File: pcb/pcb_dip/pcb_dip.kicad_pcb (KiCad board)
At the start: 2 copper layers, 67.3 x 43.2 mm, 20 parts, among them J1 USB_B_Micro, J4 Barrel_Jack, SW1 MODE, SW2 UP, SW3 DOWN, U1 ATmega328P-PU, U2 MPXV5010, U3 LTC-4627, Y1 Resonator_Small

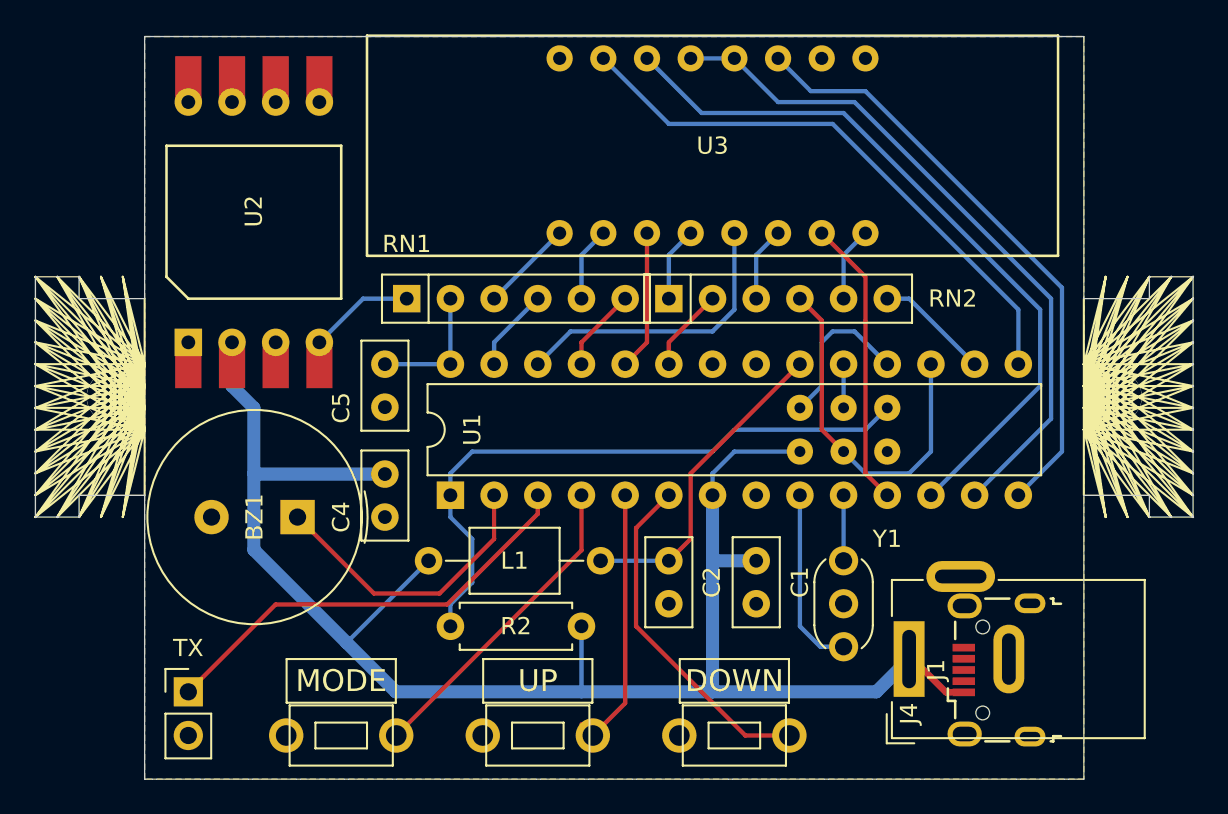
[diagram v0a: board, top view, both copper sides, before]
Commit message: better ground plane
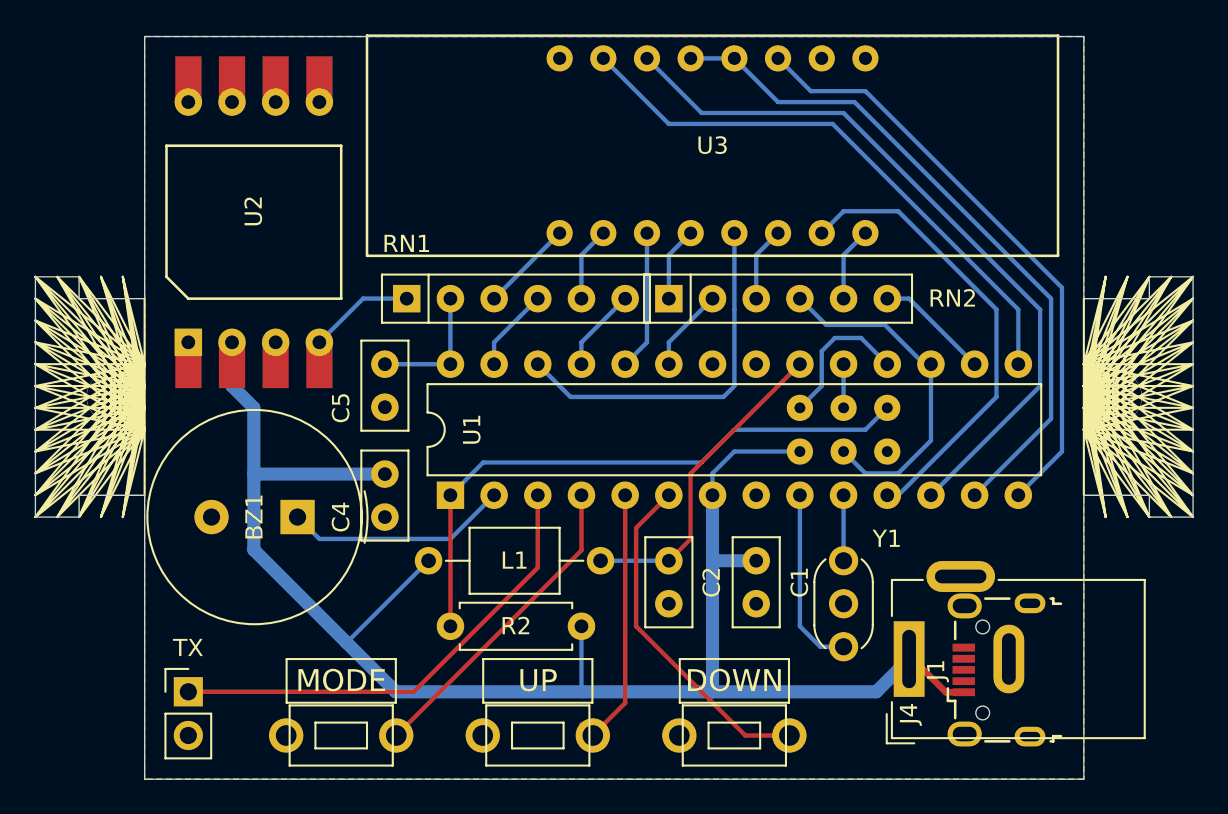
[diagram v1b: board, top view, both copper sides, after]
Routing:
- net /DP: track 16.8 -> 26.9 mm
- net Net-(BZ1-Pad1): track 17.3 -> 13.0 mm
- net /e: track 17.2 -> 21.4 mm
- net Net-(J3-Pad1): track 25.7 -> 27.5 mm
- net /RST: track 36.9 -> 35.1 mm
- net /DIG3: track 21.2 -> 20.0 mm
- net /MISO: track 9.20 -> 8.58 mm
